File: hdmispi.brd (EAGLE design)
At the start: 30.5 x 25.4 mm, 3 parts

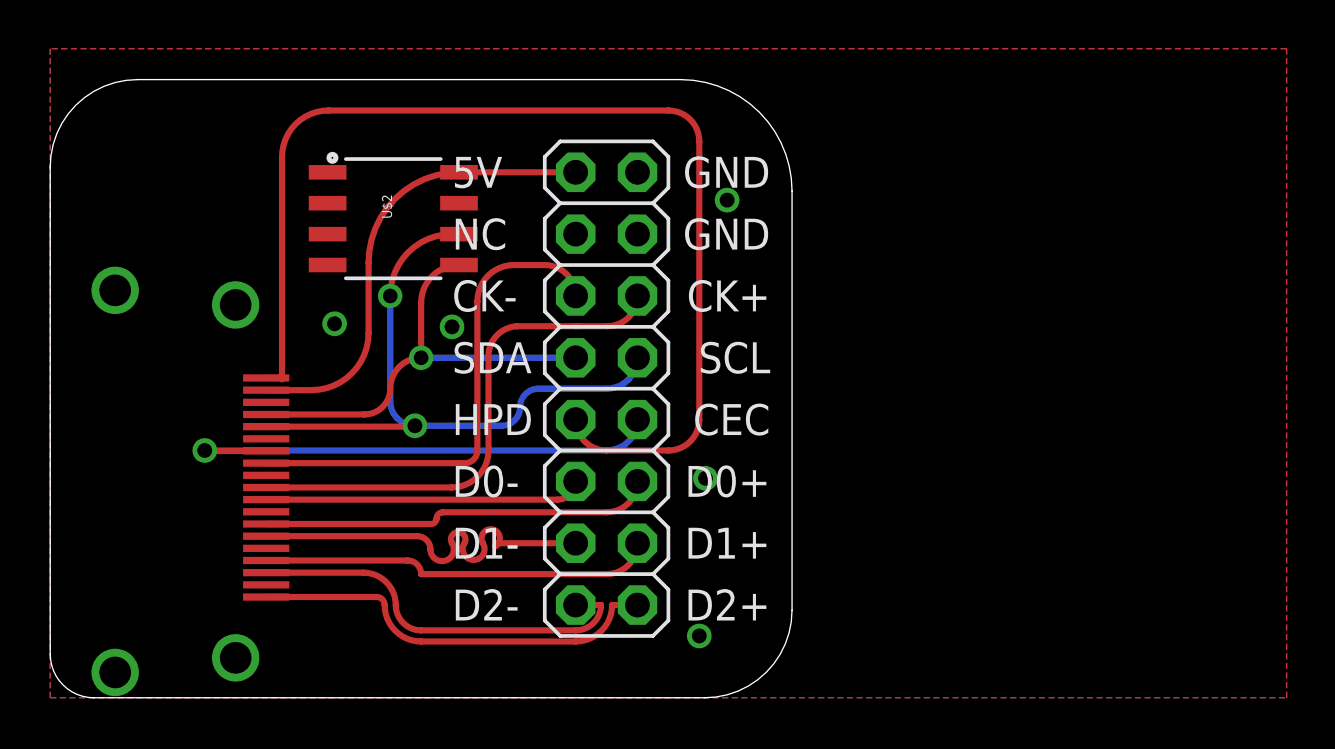
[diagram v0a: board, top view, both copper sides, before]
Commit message: Modified to use a male hdmi splint connector that straddles the edge of the pcb. no longer a full breeakout, only the bare essentials for i2c work
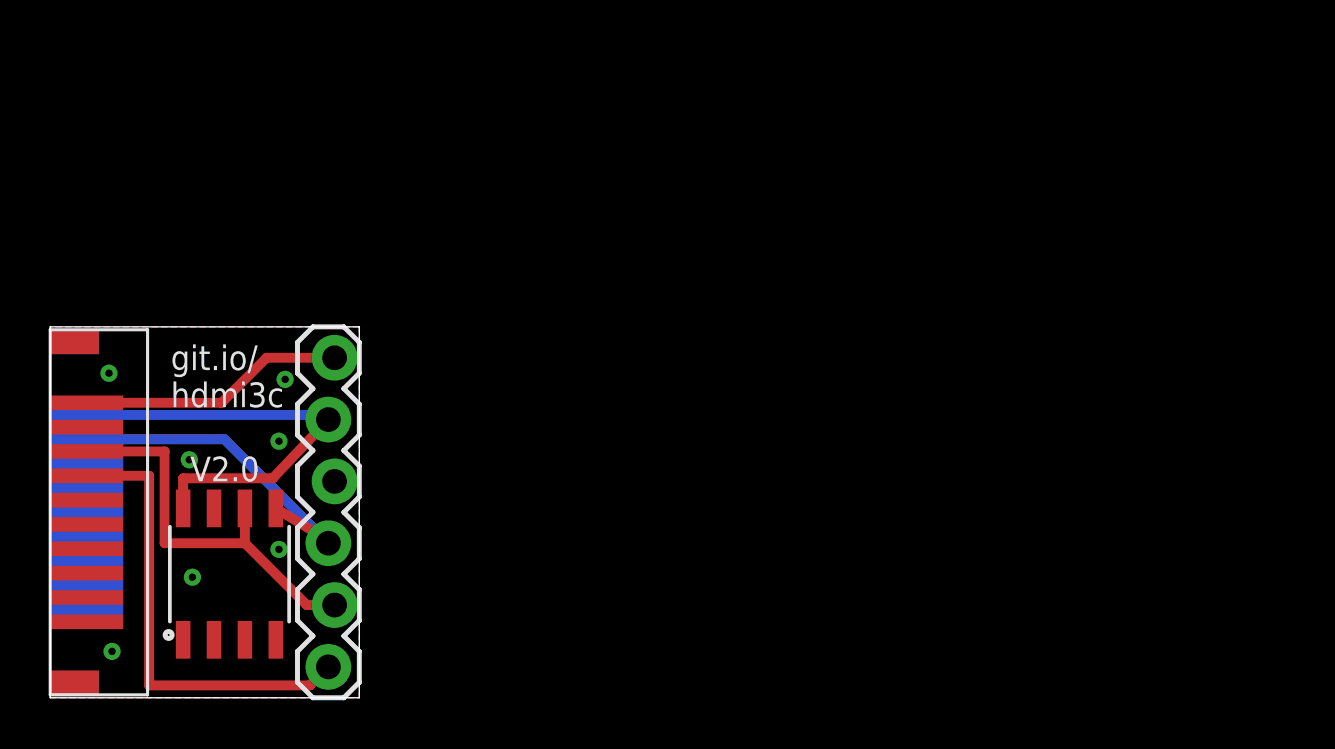
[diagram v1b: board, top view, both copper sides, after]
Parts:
- JP1: value (none) -> 0; device pinhead:2X08 -> SparkFun-Connectors:1X06-SIP_LOCK
- U$1: value HDMI -> HDMIMALE-SPLINT; device hdmispi:HDMI -> hdmispi:HDMI-MALE-SPLINT
- moved JP1 16.2 mm to (11.4, 1.27), turned to 90 degrees
- moved U$2 16.1 mm to (7.37, 5.08), turned to 0 degrees
- moved U$1 7.73 mm to (0.00, 7.62), turned to 90 degrees
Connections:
- removed net CEC: JP1.10, U$1.P$13
- removed net DETECT: JP1.9, U$1.P$19
- removed net TMDS0_N: JP1.11, U$1.P$9
- removed net TMDS0_P: JP1.12, U$1.P$7
- removed net TMDS1_N: JP1.13, U$1.P$6
- removed net TMDS1_P: JP1.14, U$1.P$4
- removed net TMDS2_N: JP1.15, U$1.P$3
- removed net TMDS2_P: JP1.16, U$1.P$1
- removed net TMDSC_N: JP1.5, U$1.P$12
- removed net TMDSC_P: JP1.6, U$1.P$10
- new net N$1: JP1.6, U$1.P$19
- new net N$3: JP1.1, U$1.P$13
- net 5V: now also JP1.5; no longer JP1.1
- net DDC_CK: now also JP1.2; no longer JP1.8
- net DDC_D: now also JP1.3; no longer JP1.7
- net GND: no longer JP1.2
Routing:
- net DETECT: track 45.9 -> 0.00 mm
- net CEC: track 20.8 -> 0.00 mm, vias 1 -> 0
- net TMDSC_P: track 20.8 -> 0.00 mm
- net TMDSC_N: track 20.2 -> 0.00 mm
- net N$3: track 0.00 -> 18.9 mm
- net TMDS2_P: track 16.6 -> 0.00 mm
- net TMDS2_N: track 16.2 -> 0.00 mm
- net TMDS1_P: track 16.0 -> 0.00 mm
- net TMDS0_P: track 16.0 -> 0.00 mm
- net TMDS1_N: track 13.0 -> 0.00 mm
- net TMDS0_N: track 13.0 -> 0.00 mm
- net N$1: track 0.00 -> 11.0 mm
- net DDC_CK: track 26.1 -> 16.4 mm, vias 2 -> 0
- net DDC_D: track 18.1 -> 14.3 mm, vias 1 -> 0
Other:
- board size 30.5 x 25.4 mm -> 12.7 x 15.2 mm
- board text added: "HPD 5V GND SDA SCL CEC"
- board text added: "git.io/ hdmi3c V2.0"
- board text removed: "5V NC CK- SDA HPD D0- D1- D2-"
- board text removed: "GND GND CK+ SCL CEC D0+ D1+ D2+"
- board text removed: "joefitz@securinghardware.com HDMI Breakout v1.1 W/ Microchip 24LC00/SN I2C EEPROM for EDID"

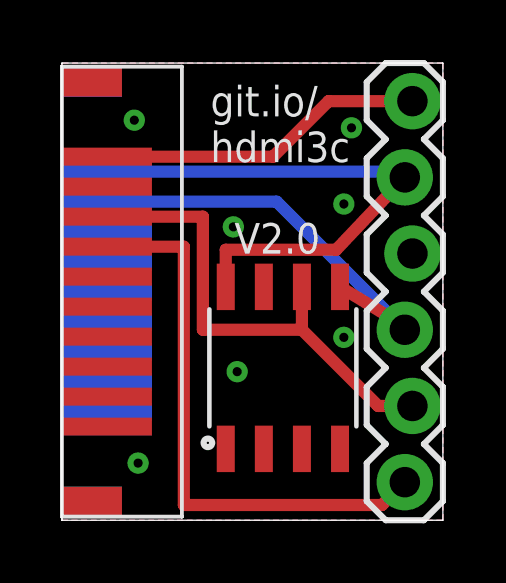
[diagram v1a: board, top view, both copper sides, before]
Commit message: fixing full pin swizzle on hdmi port. this one should actually work.
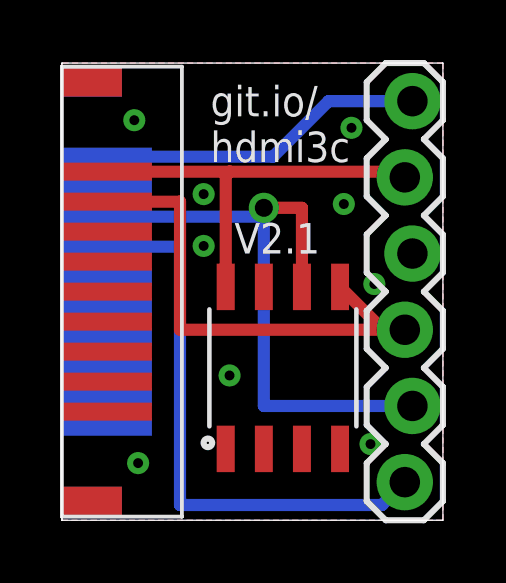
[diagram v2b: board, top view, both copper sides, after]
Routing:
- net 5V: track 18.3 -> 13.9 mm
- net DDC_CK: track 16.4 -> 20.7 mm, vias 0 -> 1
- net DDC_D: track 14.3 -> 17.0 mm
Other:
- board text added: "git.io/ hdmi3c V2.1"
- board text removed: "git.io/ hdmi3c V2.0"
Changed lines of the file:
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@@
 <text x="4.953" y="11.684" size="1.016" layer="25" font="vector" align="center-left">git.io/
 hdmi3c
-  V2.0</text>
+  V2.1</text>
 <text x="5.461" y="7.62" size="1.27" layer="26" font="vector" distance="100" rot="MR180" align="center-left">HPD
 5V
@@
 <contactref element="U$2" pad="8"/>
 <contactref element="JP1" pad="5"/>
-<wire x1="1.5" y1="11.62" x2="11.24" y2="11.62" width="0.4064" layer="16"/>
-<wire x1="11.24" y1="11.62" x2="11.43" y2="11.43" width="0.4064" layer="16"/>
-<wire x1="11.43" y1="11.43" x2="9.144" y2="9.017" width="0.4064" layer="1"/>
-<wire x1="5.461" y1="7.78" x2="5.461" y2="9.017" width="0.4064" layer="1"/>
-<wire x1="5.461" y1="9.017" x2="9.144" y2="9.017" width="0.4064" layer="1"/>
+<wire x1="1.5" y1="11.62" x2="5.588" y2="11.62" width="0.4064" layer="1"/>
+<wire x1="5.588" y1="11.62" x2="11.24" y2="11.62" width="0.4064" layer="1"/>
+<wire x1="11.24" y1="11.62" x2="11.43" y2="11.43" width="0.4064" layer="1"/>
+<wire x1="5.461" y1="7.78" x2="5.461" y2="11.493" width="0.4064" layer="1"/>
+<wire x1="5.461" y1="11.493" x2="5.588" y2="11.62" width="0.4064" layer="1"/>
 </signal>
 <signal name="GND">
@@
 <contactref element="U$1" pad="P$20"/>
 <contactref element="JP1" pad="4"/>
-<via x="2.413" y="13.335" extent="1-16" drill="0.3048" diameter="0.254"/>
-<via x="9.652" y="13.081" extent="1-16" drill="0.3048" diameter="0.254"/>
-<via x="9.398" y="10.541" extent="1-16" drill="0.3048" diameter="0.254"/>
-<via x="5.715" y="9.779" extent="1-16" drill="0.3048" diameter="0.254"/>
-<via x="2.54" y="1.905" extent="1-16" drill="0.3048" diameter="0.254"/>
-<via x="5.842" y="4.953" extent="1-16" drill="0.3048" diameter="0.254"/>
-<via x="9.398" y="6.096" extent="1-16" drill="0.3048" diameter="0.254"/>
+<via x="2.413" y="13.335" extent="1-16" drill="0.3302" diameter="0.254"/>
+<via x="9.652" y="13.081" extent="1-16" drill="0.3302" diameter="0.254"/>
+<via x="9.398" y="10.541" extent="1-16" drill="0.3302" diameter="0.254"/>
+<via x="4.7244" y="10.8712" extent="1-16" drill="0.3302" diameter="0.254"/>
+<via x="2.54" y="1.905" extent="1-16" drill="0.3302" diameter="0.254"/>
+<via x="10.287" y="2.54" extent="1-16" drill="0.3302" diameter="0.254"/>
+<via x="5.588" y="4.826" extent="1-16" drill="0.3302" diameter="0.254"/>
+<via x="4.7244" y="9.144" extent="1-16" drill="0.3302" diameter="0.254"/>
+<via x="10.414" y="7.874" extent="1-16" drill="0.3302" diameter="0.254"/>
 </signal>
 <signal name="DDC_D">
@@
 <contactref element="U$2" pad="5"/>
 <contactref element="JP1" pad="3"/>
-<wire x1="1.5" y1="10.62" x2="7.16" y2="10.62" width="0.4064" layer="16"/>
-<wire x1="7.16" y1="10.62" x2="11.43" y2="6.35" width="0.4064" layer="16"/>
-<wire x1="11.43" y1="6.35" x2="11.143" y2="6.637" width="0.4064" layer="1"/>
-<wire x1="11.143" y1="6.637" x2="9.271" y2="7.78" width="0.4064" layer="1"/>
+<wire x1="11.43" y1="6.35" x2="10.701" y2="6.35" width="0.4064" layer="1"/>
+<wire x1="10.701" y1="6.35" x2="9.271" y2="7.78" width="0.4064" layer="1"/>
+<wire x1="1.5" y1="10.62" x2="3.937" y2="10.62" width="0.4064" layer="1"/>
+<wire x1="3.937" y1="10.62" x2="3.937" y2="6.35" width="0.4064" layer="1"/>
+<wire x1="3.937" y1="6.35" x2="11.43" y2="6.35" width="0.4064" layer="1"/>
 </signal>
 <signal name="DDC_CK">
@@
 <contactref element="U$2" pad="6"/>
 <contactref element="JP1" pad="2"/>
-<wire x1="1.5" y1="10.12" x2="4.699" y2="10.12" width="0.4064" layer="1"/>
-<wire x1="4.699" y1="10.12" x2="4.699" y2="6.35" width="0.4064" layer="1"/>
-<wire x1="4.699" y1="6.35" x2="8.001" y2="6.35" width="0.4064" layer="1"/>
-<wire x1="8.001" y1="6.35" x2="8.001" y2="7.78" width="0.4064" layer="1"/>
-<wire x1="11.684" y1="3.81" x2="10.541" y2="3.81" width="0.4064" layer="1"/>
-<wire x1="10.541" y1="3.81" x2="8.001" y2="6.35" width="0.4064" layer="1"/>
+<via x="6.731" y="10.414" extent="1-16" drill="0.6" shape="square"/>
+<wire x1="1.5" y1="10.12" x2="6.731" y2="10.12" width="0.4064" layer="16"/>
+<wire x1="6.731" y1="10.12" x2="6.731" y2="10.414" width="0.4064" layer="16"/>
+<wire x1="6.731" y1="10.12" x2="6.731" y2="3.81" width="0.4064" layer="16"/>
+<wire x1="6.731" y1="3.81" x2="11.684" y2="3.81" width="0.4064" layer="16"/>
+<wire x1="8.001" y1="7.78" x2="8.001" y2="10.414" width="0.4064" layer="1"/>
+<wire x1="8.001" y1="10.414" x2="6.731" y2="10.414" width="0.4064" layer="1"/>
 </signal>
 <signal name="N$1">
 <contactref element="U$1" pad="P$19"/>
 <contactref element="JP1" pad="6"/>
-<wire x1="1.5" y1="12.12" x2="7.04" y2="12.12" width="0.4064" layer="1"/>
-<wire x1="7.04" y1="12.12" x2="8.89" y2="13.97" width="0.4064" layer="1"/>
-<wire x1="8.89" y1="13.97" x2="11.684" y2="13.97" width="0.4064" layer="1"/>
+<wire x1="1.5" y1="12.12" x2="7.04" y2="12.12" width="0.4064" layer="16"/>
+<wire x1="7.04" y1="12.12" x2="8.89" y2="13.97" width="0.4064" layer="16"/>
+<wire x1="8.89" y1="13.97" x2="11.684" y2="13.97" width="0.4064" layer="16"/>
 </signal>
 <signal name="N$3">
 <contactref element="JP1" pad="1"/>
 <contactref element="U$1" pad="P$13"/>
-<wire x1="1.5" y1="9.12" x2="4.064" y2="9.12" width="0.4064" layer="1"/>
-<wire x1="4.064" y1="9.12" x2="4.064" y2="0.508" width="0.4064" layer="1"/>
-<wire x1="4.064" y1="0.508" x2="10.668" y2="0.508" width="0.4064" layer="1"/>
-<wire x1="10.668" y1="0.508" x2="11.43" y2="1.27" width="0.4064" layer="1"/>
+<wire x1="1.5" y1="9.12" x2="3.937" y2="9.12" width="0.4064" layer="16"/>
+<wire x1="3.937" y1="9.12" x2="3.937" y2="0.508" width="0.4064" layer="16"/>
+<wire x1="3.937" y1="0.508" x2="10.668" y2="0.508" width="0.4064" layer="16"/>
+<wire x1="10.668" y1="0.508" x2="11.43" y2="1.27" width="0.4064" layer="16"/>
 </signal>
 </signals>

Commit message: added micro hdmi header and revised board to match. note different pinout!!!
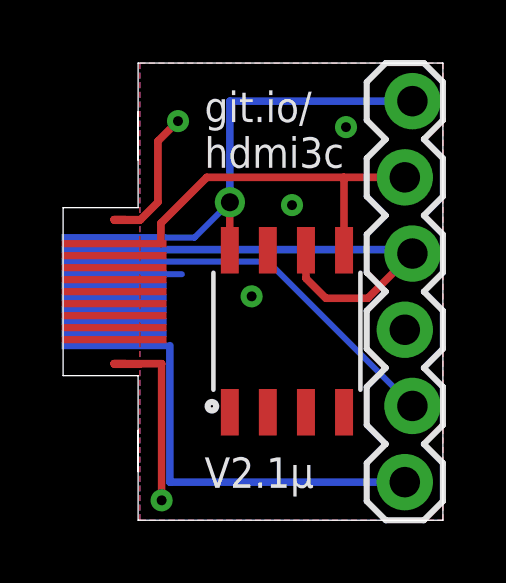
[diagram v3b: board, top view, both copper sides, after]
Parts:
- U$1: value HDMIMALE-SPLINT -> HDMIHDMI-MALE-MICRO-SPLINT; device hdmispi:HDMI-MALE-SPLINT -> hdmispi:HDMI-MALE-MICRO-SPLINT
- moved U$1 2.54 mm to (2.54, 7.62)
- moved U$2 1.23 mm to (7.50, 6.30)
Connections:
- removed net N$3: JP1.1, U$1.P$13
- new net N$2: JP1.2, U$1.P$15
- net 5V: now also JP1.6, U$1.P$19; no longer JP1.5, U$1.P$18
- net DDC_CK: now also JP1.4, U$1.P$17; no longer JP1.2, U$1.P$15
- net DDC_D: now also JP1.5, U$1.P$18; no longer JP1.3, U$1.P$16
- net GND: now also JP1.3, U$1.P$10, U$1.P$13, U$1.P$16, U$1.P$4, U$1.P$7; no longer JP1.4, U$1.P$11, U$1.P$17, U$1.P$2, U$1.P$5, U$1.P$8
- net N$1: now also JP1.1, U$1.P$1; no longer JP1.6, U$1.P$19
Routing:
- net N$3: track 18.9 -> 0.00 mm
- net GND: track 0.00 -> 15.6 mm, vias 9 -> 5
- net N$2: track 0.00 -> 11.9 mm
- net DDC_CK: track 20.7 -> 15.4 mm, vias 1 -> 0
- net DDC_D: track 17.0 -> 13.4 mm
- net N$1: track 11.0 -> 14.2 mm
- net 5V: track 13.9 -> 15.4 mm, vias 0 -> 1
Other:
- board size 12.7 x 15.2 mm -> 10.2 x 15.2 mm
- board text added: "5V SDA SCL GND CEC HPD"
- board text added: "git.io/ hdmi3c V2.1µ"
- board text removed: "HPD 5V GND SDA SCL CEC"
- board text removed: "git.io/ hdmi3c V2.1"
